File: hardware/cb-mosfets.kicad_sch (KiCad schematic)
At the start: 30 parts, among them Q901 ZXMP10A13FTA, Q902 BSS123

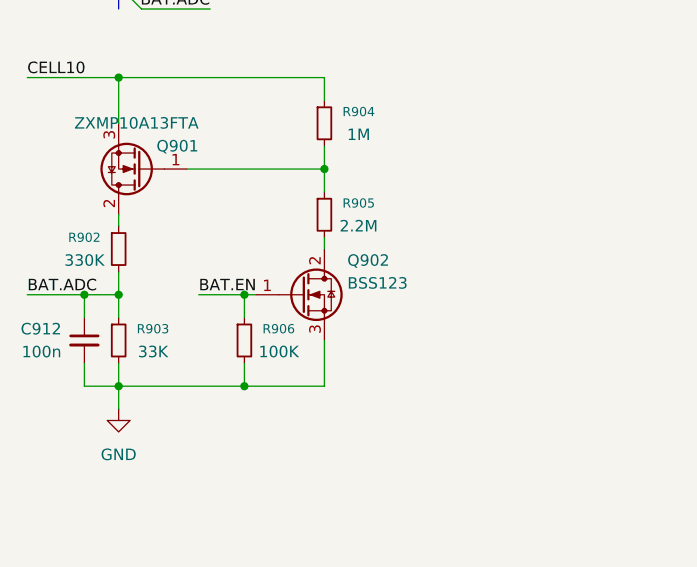
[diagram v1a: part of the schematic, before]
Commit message: reduced BOM
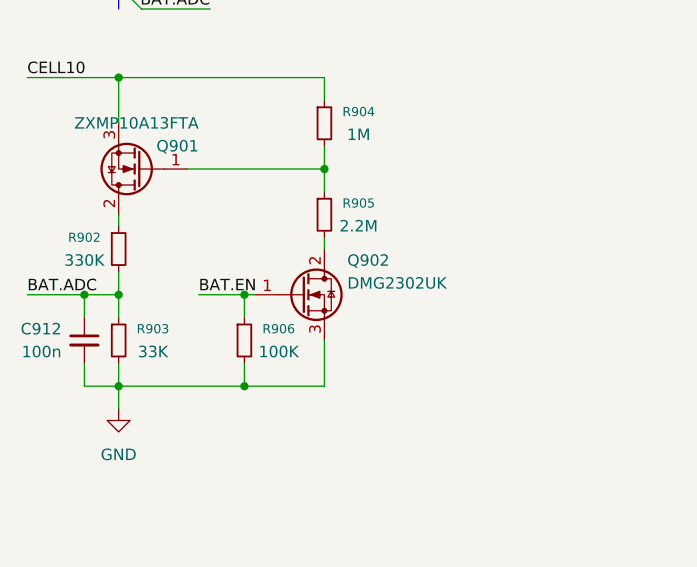
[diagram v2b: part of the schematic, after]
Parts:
- JP901, JP902, JP903, JP904, JP905: footprint (none) -> Jumper:SolderJumper-2_P1.3mm_Bridged_Pad1.0x1.5mm
- JP906, JP907, JP908: footprint (none) -> Jumper:SolderJumper-2_P1.3mm_Open_TrianglePad1.0x1.5mm
- Q902: value BSS123 -> DMG2302UK
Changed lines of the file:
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@@
 			)
 		)
-		(property "Footprint" ""
+		(property "Footprint" "Jumper:SolderJumper-2_P1.3mm_Open_TrianglePad1.0x1.5mm"
 			(at 171.45 85.09 0)
 			(hide yes)
@@
 			)
 		)
-		(property "Footprint" ""
+		(property "Footprint" "Jumper:SolderJumper-2_P1.3mm_Open_TrianglePad1.0x1.5mm"
 			(at 171.45 80.01 0)
 			(hide yes)
@@
 			)
 		)
-		(property "Footprint" ""
+		(property "Footprint" "Jumper:SolderJumper-2_P1.3mm_Bridged_Pad1.0x1.5mm"
 			(at 171.45 54.61 0)
 			(hide yes)
@@
 			)
 		)
-		(property "Footprint" ""
+		(property "Footprint" "Jumper:SolderJumper-2_P1.3mm_Open_TrianglePad1.0x1.5mm"
 			(at 171.45 74.93 0)
 			(hide yes)
@@
 			)
 		)
-		(property "Footprint" ""
+		(property "Footprint" "Jumper:SolderJumper-2_P1.3mm_Bridged_Pad1.0x1.5mm"
 			(at 171.45 64.77 0)
 			(hide yes)
@@
 			)
 		)
-		(property "Footprint" ""
+		(property "Footprint" "Jumper:SolderJumper-2_P1.3mm_Bridged_Pad1.0x1.5mm"
 			(at 171.45 59.69 0)
 			(hide yes)
@@
 			)
 		)
-		(property "Footprint" ""
+		(property "Footprint" "Jumper:SolderJumper-2_P1.3mm_Bridged_Pad1.0x1.5mm"
 			(at 171.45 49.53 0)
 			(hide yes)
@@
 			)
 		)
-		(property "Footprint" ""
+		(property "Footprint" "Jumper:SolderJumper-2_P1.3mm_Bridged_Pad1.0x1.5mm"
 			(at 171.45 69.85 0)
 			(hide yes)
@@
 			)
 		)
-		(property "Value" "BSS123"
+		(property "Value" "DMG2302UK"
 			(at 248.92 134.62 0)
 			(show_name no)

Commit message: increased size two times
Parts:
- removed C904, C905, C910: 220n, Capacitor_SMD:C_0603_1608Metric, symbol Device:C_Small
- removed JP901, JP902, JP903, JP904, JP905: SolderJumper_2_Bridged, Jumper:SolderJumper-2_P1.3mm_Bridged_Pad1.0x1.5mm, symbol Jumper:SolderJumper_2_Bridged
- removed JP906, JP907, JP908: SolderJumper_2_Open, Jumper:SolderJumper-2_P1.3mm_Open_TrianglePad1.0x1.5mm, symbol Jumper:SolderJumper_2_Open
- added R907, R908, R909: 0, Resistor_SMD:R_0603_1608Metric, symbol Device:R_Small
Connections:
- net VC6: now also R907.1
- net VC7: now also R907.2, R908.1
- net VC8: now also R908.2, R909.1
- net VC9: now also R909.2
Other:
- note added: "Instead of jumper: We could try change C to 0R that joins VC3-9. But required adjustment of Fuse3T"
- note removed: "Preconnected jumpers"

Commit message: some chnages
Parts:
- Q902: value DMG2302UK -> 2N7002K
